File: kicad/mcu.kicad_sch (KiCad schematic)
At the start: 16 parts, among them U2 DSC1001DI1-025.0000T, U4 RP2040

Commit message: Connected all remaining unconnected pins
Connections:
- net SDA_0: now reaches U4.11 (GPIO8)
- net SCL_0: now reaches U4.12 (GPIO9)
- net GPIO_CD: now reaches U4.13 (GPIO10)
- net GPIO_23: now reaches U4.14 (GPIO11)
- net GPIO_11: now reaches U4.15 (GPIO12)
- net GPIO_10: now reaches U4.16 (GPIO13)
- net GPIO_9: now reaches U4.17 (GPIO14)
- net GPIO_8: now reaches U4.18 (GPIO15)
- net GPIO_8: now also U4.37 (GPIO25)
- net SWCIK: now reaches U4.24 (SWCLK)
- net SWDIO: now reaches U4.25 (SWDIO)
- net GPIO_1: now reaches U4.29 (GPIO18)
- net GPIO_2: now reaches U4.30 (GPIO19)
- net GPIO_3: now reaches U4.31 (GPIO20)
- net GPIO_4: now reaches U4.32 (GPIO21)
- net GPIO_5: now reaches U4.34 (GPIO22)
- net GPIO_6: now reaches U4.35 (GPIO23)
- net GPIO_7: now reaches U4.36 (GPIO24)
- net GPIO_14_A3: now reaches U4.39 (GPIO27/ADC1)
- net GPIO_13_A2: now reaches U4.40 (GPIO28/ADC2)
- net GPIO_12_A1: now reaches U4.41 (GPIO29/ADC3)
- net QSPI_SS: now reaches U4.56 (QSPI_SS_N)
- net SDA_1: now reaches U4.8 (GPIO6)
- net SCL_1: now reaches U4.9 (GPIO7)
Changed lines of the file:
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@@
+    )
+  )
+  (global_label "SDA_1" (shape input) (at 68.58 72.39 180) (fields_autoplaced)
+    (effects (font (size 1.27 1.27)) (justify right))
+    (property "Intersheet References" "${INTERSHEET_REFS}" (id 0) (at 60.4217 72.3106 0)
+      (effects (font (size 1.27 1.27)) (justify right) hide)
+    )
+  )
+  (global_label "SWCIK" (shape output) (at 68.58 113.03 180) (fields_autoplaced)
+    (effects (font (size 1.27 1.27)) (justify right))
+    (property "Intersheet References" "${INTERSHEET_REFS}" (id 0) (at 60.3612 112.9506 0)
+      (effects (font (size 1.27 1.27)) (justify right) hide)
     )
   )
@@
     )
   )
+  (global_label "GPIO_12_A1" (shape bidirectional) (at 129.54 95.25 0) (fields_autoplaced)
+    (effects (font (size 1.27 1.27)) (justify left))
+    (property "Intersheet References" "${INTERSHEET_REFS}" (id 0) (at 143.0807 95.3294 0)
+      (effects (font (size 1.27 1.27)) (justify left) hide)
+    )
+  )
   (global_label "DN" (shape bidirectional) (at 153.67 82.55 0) (fields_autoplaced)
     (effects (font (size 1.27 1.27)) (justify left))
@@
     )
   )
+  (global_label "SDA_0" (shape input) (at 68.58 80.01 180) (fields_autoplaced)
+    (effects (font (size 1.27 1.27)) (justify right))
+    (property "Intersheet References" "${INTERSHEET_REFS}" (id 0) (at 60.4217 79.9306 0)
+      (effects (font (size 1.27 1.27)) (justify right) hide)
+    )
+  )
+  (global_label "GPIO_4" (shape bidirectional) (at 129.54 118.11 0) (fields_autoplaced)
+    (effects (font (size 1.27 1.27)) (justify left))
+    (property "Intersheet References" "${INTERSHEET_REFS}" (id 0) (at 138.6055 118.0306 0)
+      (effects (font (size 1.27 1.27)) (justify left) hide)
+    )
+  )
+  (global_label "QSPI_SS" (shape input) (at 129.54 57.15 0) (fields_autoplaced)
+    (effects (font (size 1.27 1.27)) (justify left))
+    (property "Intersheet References" "${INTERSHEET_REFS}" (id 0) (at 139.7545 57.0706 0)
+      (effects (font (size 1.27 1.27)) (justify left) hide)
+    )
+  )
   (global_label "QSPI_SD1" (shape bidirectional) (at 129.54 59.69 0) (fields_autoplaced)
     (effects (font (size 1.27 1.27)) (justify left))
@@
     )
   )
+  (global_label "SWDIO" (shape bidirectional) (at 68.58 115.57 180) (fields_autoplaced)
+    (effects (font (size 1.27 1.27)) (justify right))
+    (property "Intersheet References" "${INTERSHEET_REFS}" (id 0) (at 60.3007 115.6494 0)
+      (effects (font (size 1.27 1.27)) (justify right) hide)
+    )
+  )
+  (global_label "GPIO_13_A2" (shape bidirectional) (at 129.54 97.79 0) (fields_autoplaced)
+    (effects (font (size 1.27 1.27)) (justify left))
+    (property "Intersheet References" "${INTERSHEET_REFS}" (id 0) (at 143.0807 97.8694 0)
+      (effects (font (size 1.27 1.27)) (justify left) hide)
+    )
+  )
   (global_label "SD_DAT1" (shape bidirectional) (at 68.58 59.69 180) (fields_autoplaced)
     (effects (font (size 1.27 1.27)) (justify right))
@@
     )
   )
+  (global_label "GPIO_6" (shape bidirectional) (at 129.54 110.49 0) (fields_autoplaced)
+    (effects (font (size 1.27 1.27)) (justify left))
+    (property "Intersheet References" "${INTERSHEET_REFS}" (id 0) (at 138.6055 110.4106 0)
+      (effects (font (size 1.27 1.27)) (justify left) hide)
+    )
+  )
+  (global_label "GPIO_9" (shape bidirectional) (at 68.58 95.25 180) (fields_autoplaced)
+    (effects (font (size 1.27 1.27)) (justify right))
+    (property "Intersheet References" "${INTERSHEET_REFS}" (id 0) (at 59.5145 95.1706 0)
+      (effects (font (size 1.27 1.27)) (justify right) hide)
+    )
+  )
+  (global_label "GPIO_11" (shape bidirectional) (at 68.58 90.17 180) (fields_autoplaced)
+    (effects (font (size 1.27 1.27)) (justify right))
+    (property "Intersheet References" "${INTERSHEET_REFS}" (id 0) (at 58.305 90.0906 0)
+      (effects (font (size 1.27 1.27)) (justify right) hide)
+    )
+  )
+  (global_label "SCL_0" (shape input) (at 68.58 82.55 180) (fields_autoplaced)
+    (effects (font (size 1.27 1.27)) (justify right))
+    (property "Intersheet References" "${INTERSHEET_REFS}" (id 0) (at 60.4821 82.4706 0)
+      (effects (font (size 1.27 1.27)) (justify right) hide)
+    )
+  )
+  (global_label "GPIO_7" (shape bidirectional) (at 129.54 107.95 0) (fields_autoplaced)
+    (effects (font (size 1.27 1.27)) (justify left))
+    (property "Intersheet References" "${INTERSHEET_REFS}" (id 0) (at 138.6055 107.8706 0)
+      (effects (font (size 1.27 1.27)) (justify left) hide)
+    )
+  )
+  (global_label "GPIO_8" (shape bidirectional) (at 68.58 97.79 180) (fields_autoplaced)
+    (effects (font (size 1.27 1.27)) (justify right))
+    (property "Intersheet References" "${INTERSHEET_REFS}" (id 0) (at 59.5145 97.7106 0)
+      (effects (font (size 1.27 1.27)) (justify right) hide)
+    )
+  )
   (global_label "SD_DAT0" (shape bidirectional) (at 68.58 57.15 180) (fields_autoplaced)
     (effects (font (size 1.27 1.27)) (justify right))
@@
     )
   )
+  (global_label "GPIO_3" (shape bidirectional) (at 129.54 120.65 0) (fields_autoplaced)
+    (effects (font (size 1.27 1.27)) (justify left))
+    (property "Intersheet References" "${INTERSHEET_REFS}" (id 0) (at 138.6055 120.5706 0)
+      (effects (font (size 1.27 1.27)) (justify left) hide)
+    )
+  )
+  (global_label "GPIO_14_A3" (shape bidirectional) (at 129.54 100.33 0) (fields_autoplaced)
+    (effects (font (size 1.27 1.27)) (justify left))
+    (property "Intersheet References" "${INTERSHEET_REFS}" (id 0) (at 143.0807 100.4094 0)
+      (effects (font (size 1.27 1.27)) (justify left) hide)
+    )
+  )
   (global_label "QSPI_SCLK" (shape input) (at 129.54 67.31 0) (fields_autoplaced)
     (effects (font (size 1.27 1.27)) (justify left))
@@
     )
   )
+  (global_label "GPIO_10" (shape bidirectional) (at 68.58 92.71 180) (fields_autoplaced)
+    (effects (font (size 1.27 1.27)) (justify right))
+    (property "Intersheet References" "${INTERSHEET_REFS}" (id 0) (at 58.305 92.6306 0)
+      (effects (font (size 1.27 1.27)) (justify right) hide)
+    )
+  )
   (global_label "SD_DAT3" (shape bidirectional) (at 68.58 64.77 180) (fields_autoplaced)
     (effects (font (size 1.27 1.27)) (justify right))
@@
     )
   )
+  (global_label "GPIO_1" (shape bidirectional) (at 129.54 125.73 0) (fields_autoplaced)
+    (effects (font (size 1.27 1.27)) (justify left))
+    (property "Intersheet References" "${INTERSHEET_REFS}" (id 0) (at 138.6055 125.6506 0)
+      (effects (font (size 1.27 1.27)) (justify left) hide)
+    )
+  )
   (global_label "GPIO_TEMP" (shape input) (at 129.54 102.87 0) (fields_autoplaced)
     (effects (font (size 1.27 1.27)) (justify left))
@@
     )
   )
+  (global_label "GPIO_8" (shape bidirectional) (at 129.54 105.41 0) (fields_autoplaced)
+    (effects (font (size 1.27 1.27)) (justify left))
+    (property "Intersheet References" "${INTERSHEET_REFS}" (id 0) (at 138.6055 105.3306 0)
+      (effects (font (size 1.27 1.27)) (justify left) hide)
+    )
+  )
+  (global_label "GPIO_2" (shape bidirectional) (at 129.54 123.19 0) (fields_autoplaced)
+    (effects (font (size 1.27 1.27)) (justify left))
+    (property "Intersheet References" "${INTERSHEET_REFS}" (id 0) (at 138.6055 123.1106 0)
+      (effects (font (size 1.27 1.27)) (justify left) hide)
+    )
+  )
   (global_label "SD_CMD" (shape bidirectional) (at 68.58 67.31 180) (fields_autoplaced)
     (effects (font (size 1.27 1.27)) (justify right))
@@
     )
   )
+  (global_label "SCL_1" (shape input) (at 68.58 74.93 180) (fields_autoplaced)
+    (effects (font (size 1.27 1.27)) (justify right))
+    (property "Intersheet References" "${INTERSHEET_REFS}" (id 0) (at 60.4821 74.8506 0)
+      (effects (font (size 1.27 1.27)) (justify right) hide)
+    )
+  )
+  (global_label "GPIO_23" (shape bidirectional) (at 68.58 87.63 180) (fields_autoplaced)
+    (effects (font (size 1.27 1.27)) (justify right))
+    (property "Intersheet References" "${INTERSHEET_REFS}" (id 0) (at 58.305 87.5506 0)
+      (effects (font (size 1.27 1.27)) (justify right) hide)
+    )
+  )
   (global_label "GPIO_CAN_TXD" (shape input) (at 68.58 120.65 180) (fields_autoplaced)
     (effects (font (size 1.27 1.27)) (justify right))
@@
     )
   )
+  (global_label "GPIO_CD" (shape input) (at 68.58 85.09 180) (fields_autoplaced)
+    (effects (font (size 1.27 1.27)) (justify right))
+    (property "Intersheet References" "${INTERSHEET_REFS}" (id 0) (at 58.184 85.0106 0)
+      (effects (font (size 1.27 1.27)) (justify right) hide)
+    )
+  )
+  (global_label "GPIO_5" (shape bidirectional) (at 129.54 113.03 0) (fields_autoplaced)
+    (effects (font (size 1.27 1.27)) (justify left))
+    (property "Intersheet References" "${INTERSHEET_REFS}" (id 0) (at 138.6055 112.9506 0)
+      (effects (font (size 1.27 1.27)) (justify left) hide)
+    )
+  )

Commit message: Updated schematic with various changes
Increased size of small components
Updated title/spec sheet
Cleaned footprints
Other small changes as well
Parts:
- C1: renamed from C7; footprint personal:C_0201_0603Metric -> personal:C_0402_1005Metric
- C10: renamed from C16; footprint personal:C_0201_0603Metric -> personal:C_0402_1005Metric
- C11: renamed from C18; footprint personal:C_0201_0603Metric -> personal:C_0402_1005Metric
- C12: renamed from C19; footprint personal:C_0201_0603Metric -> personal:C_0402_1005Metric
- C2: renamed from C8; footprint personal:C_0201_0603Metric -> personal:C_0402_1005Metric
- C3: renamed from C9; footprint personal:C_0201_0603Metric -> personal:C_0402_1005Metric
- C4: renamed from C10; footprint personal:C_0201_0603Metric -> personal:C_0402_1005Metric
- C5: renamed from C11; footprint personal:C_0201_0603Metric -> personal:C_0402_1005Metric
- C6: renamed from C12; footprint personal:C_0201_0603Metric -> personal:C_0402_1005Metric
- C7: renamed from C13; footprint personal:C_0201_0603Metric -> personal:C_0402_1005Metric
- C8: renamed from C14; footprint personal:C_0201_0603Metric -> personal:C_0402_1005Metric
- C9: renamed from C15; footprint personal:C_0201_0603Metric -> personal:C_0402_1005Metric
- R1: renamed from R2; footprint personal:R_0201_0603Metric -> personal:R_0402_1005Metric
- R2: renamed from R3; footprint personal:R_0201_0603Metric -> personal:R_0402_1005Metric
- renumbered U4 to U1
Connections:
- net GPIO_CAN_TXD: no longer U1.28 (GPIO17)
- new net GPIO_CAN_RXD: U1.28 (GPIO17)

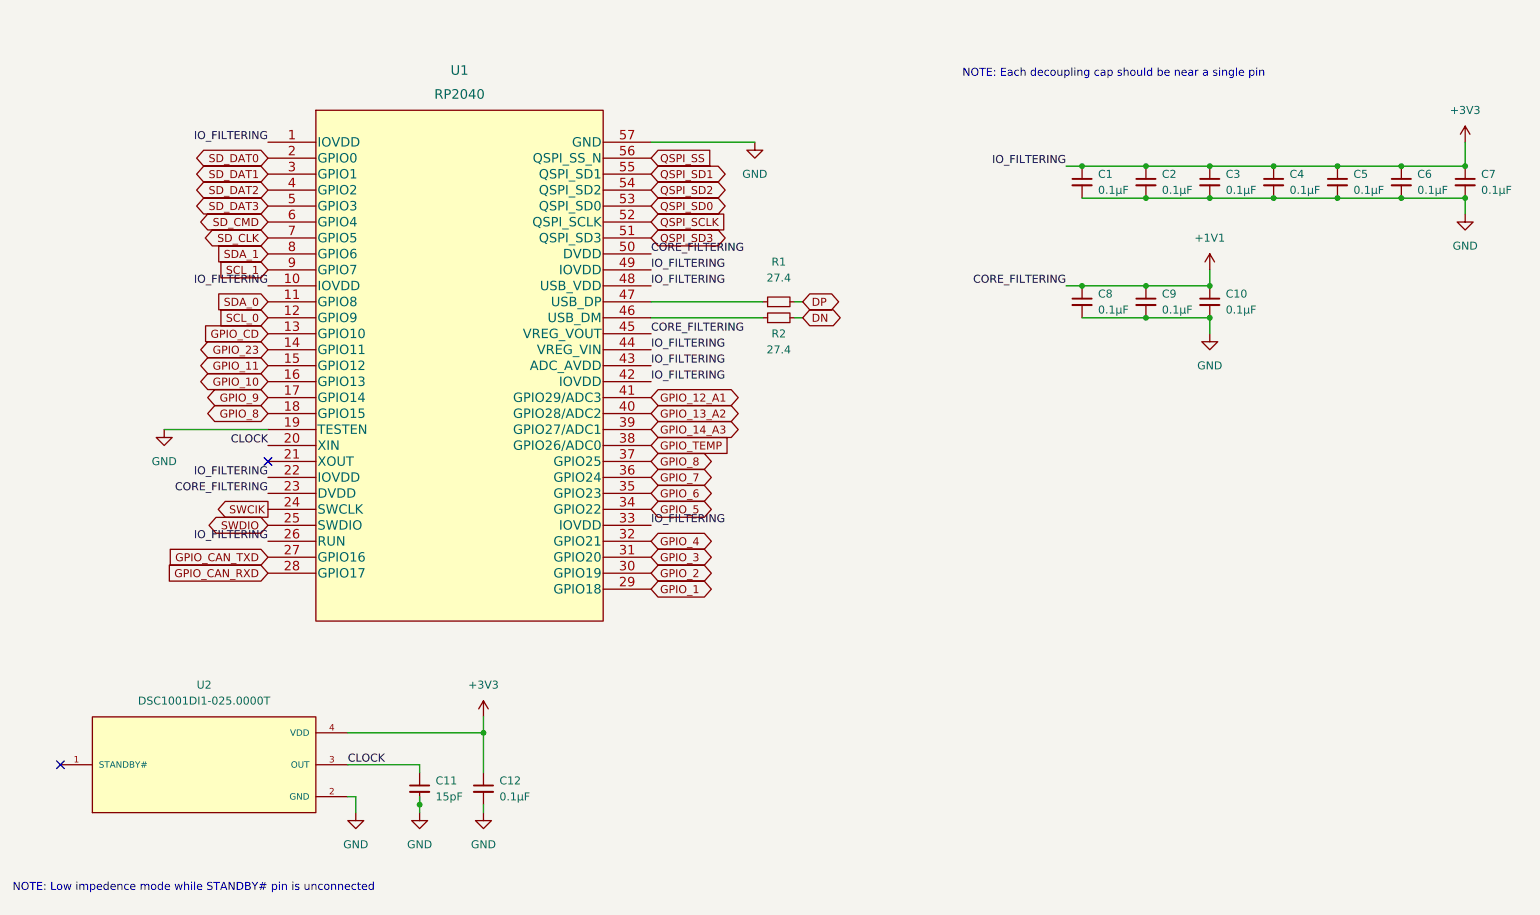
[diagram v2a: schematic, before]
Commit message: Changed pinout on main pcb connector
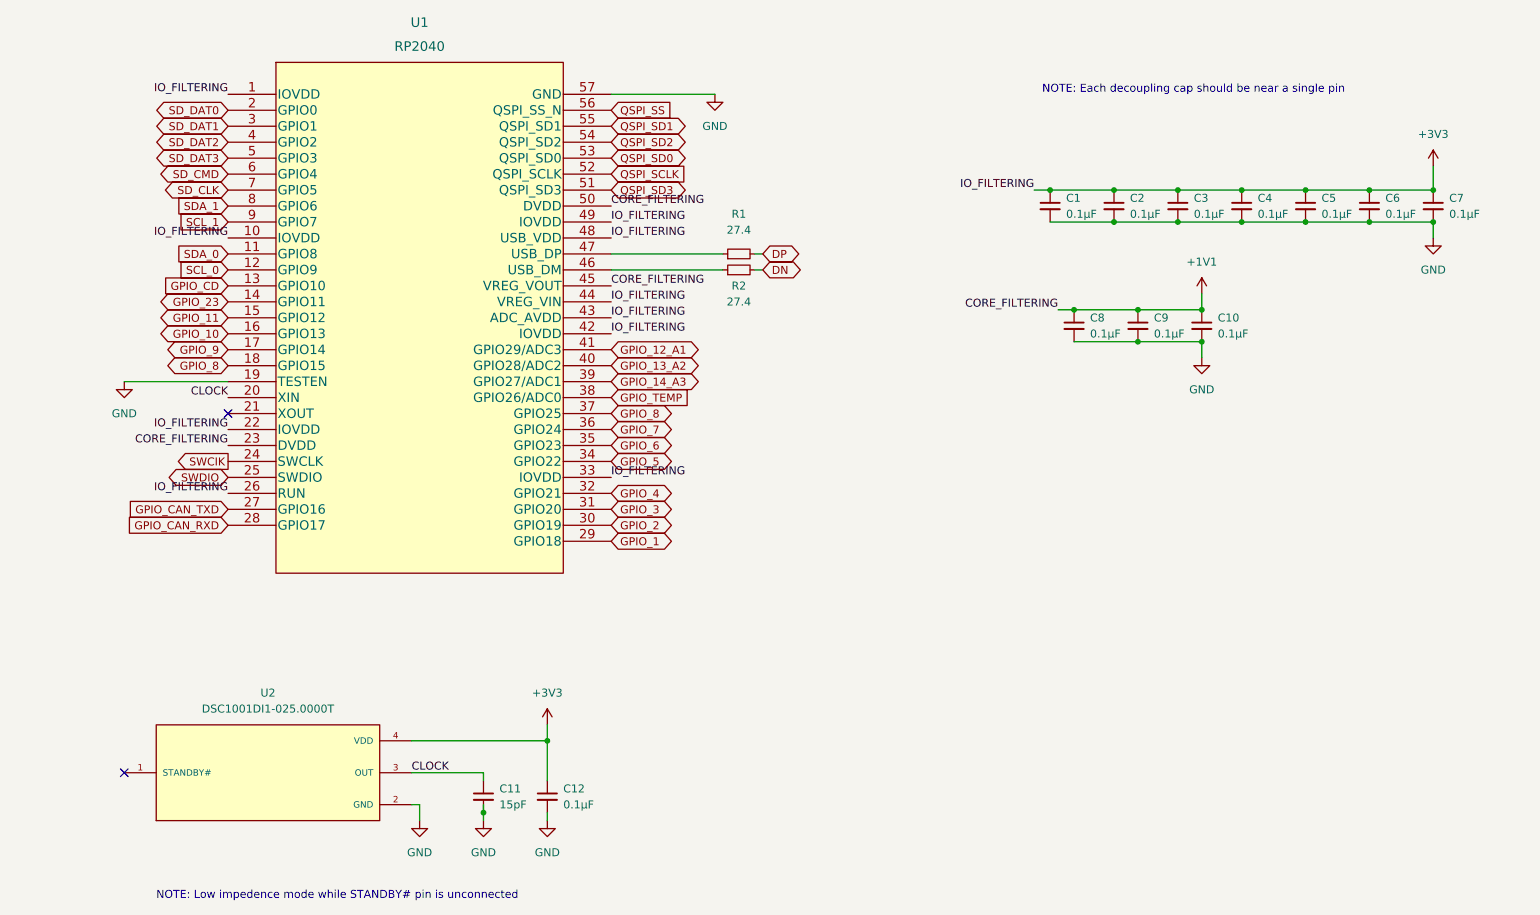
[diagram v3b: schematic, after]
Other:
- moved on the sheet: C1, C10, C11, C12, C2, C3, C4, C5, C6, C7, C8, C9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
